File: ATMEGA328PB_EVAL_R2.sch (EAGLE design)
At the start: 13 parts, among them U2 ATMEGA328PB-AU

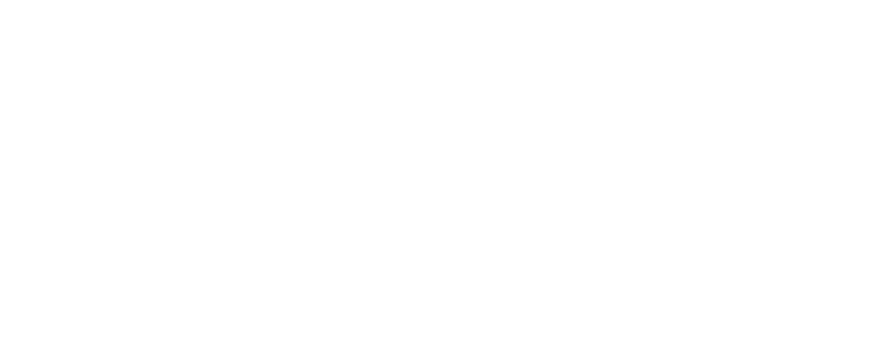
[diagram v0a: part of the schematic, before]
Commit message: Added License and schematic PDF
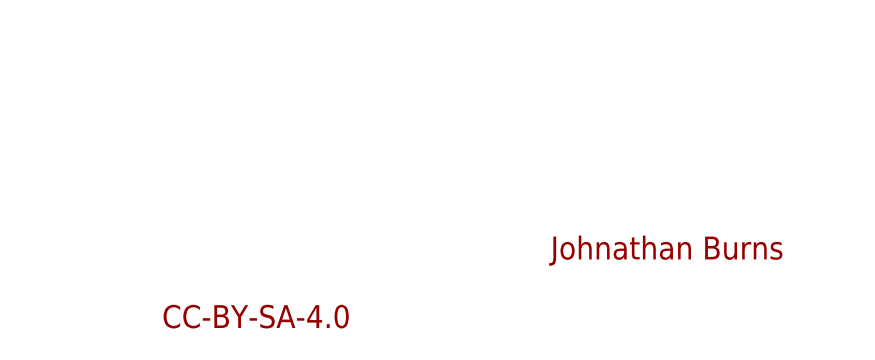
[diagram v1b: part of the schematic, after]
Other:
- note added: "CC-BY-SA-4.0"
- note added: "Johnathan Burns"
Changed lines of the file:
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@@
 <sheet>
 <plain>
+<text x="218.44" y="20.32" size="2.54" layer="94">Johnathan Burns</text>
+<text x="175.26" y="12.7" size="2.54" layer="94">CC-BY-SA-4.0</text>
 </plain>
 <instances>
